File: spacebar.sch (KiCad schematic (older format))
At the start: 5 parts

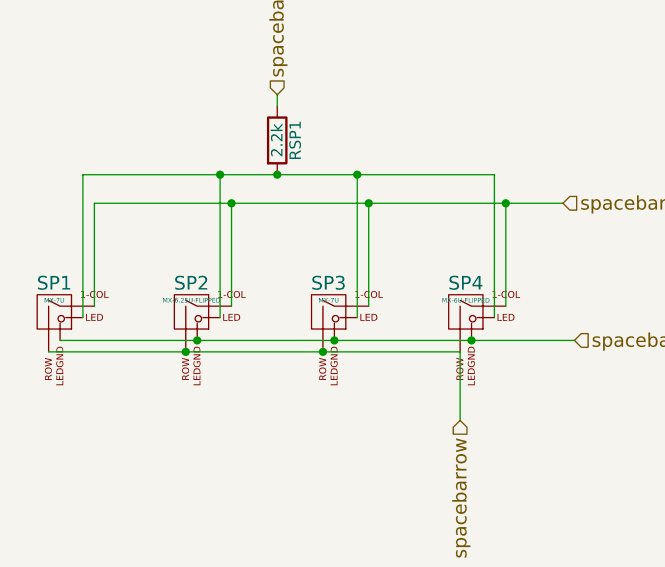
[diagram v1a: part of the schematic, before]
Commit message: Fix all key annotations
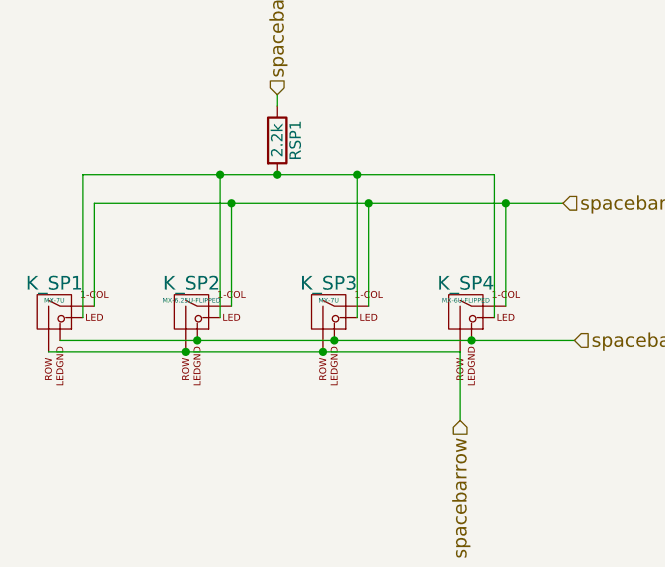
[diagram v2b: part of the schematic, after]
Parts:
- renumbered SP1 to K_SP1, SP2 to K_SP2, SP3 to K_SP3, SP4 to K_SP4
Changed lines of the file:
@@
 $EndDescr
 $Comp
-L MX-7U SP1
+L MX-7U K_SP1
 U 1 1 59353DBD
 P 3825 3400
-F 0 "SP1" H 3825 3525 60  0000 C CNN
+F 0 "K_SP1" H 3825 3525 60  0000 C CNN
 F 1 "MX-7U" H 3825 3450 20  0000 C CNN
 F 2 "" H 3800 3375 60  0001 C CNN
@@
 $EndComp
 $Comp
-L MX-7U SP3
+L MX-7U K_SP3
 U 1 1 59353E7D
 P 5025 3400
-F 0 "SP3" H 5025 3525 60  0000 C CNN
+F 0 "K_SP3" H 5025 3525 60  0000 C CNN
 F 1 "MX-7U" H 5025 3450 20  0000 C CNN
 F 2 "" H 5000 3375 60  0001 C CNN
@@
 	4800 2500 4800 2450
 $Comp
-L MX-6.25U-FLIPPED SP2
+L MX-6.25U-FLIPPED K_SP2
 U 1 1 593599DE
 P 4425 3400
-F 0 "SP2" H 4425 3525 60  0000 C CNN
+F 0 "K_SP2" H 4425 3525 60  0000 C CNN
 F 1 "MX-6.25U-FLIPPED" H 4425 3450 20  0000 C CNN
 F 2 "" H 4400 3375 60  0001 C CNN
@@
 Connection ~ 4450 3525
 $Comp
-L MX-6U-FLIPPED SP4
+L MX-6U-FLIPPED K_SP4
 U 1 1 59359F3B
 P 5625 3400
-F 0 "SP4" H 5625 3525 60  0000 C CNN
+F 0 "K_SP4" H 5625 3525 60  0000 C CNN
 F 1 "MX-6U-FLIPPED" H 5625 3450 20  0000 C CNN
 F 2 "" H 5600 3375 60  0001 C CNN

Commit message: Fix left shift, associate MX footprints
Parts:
- K_SP1, K_SP3: footprint (none) -> MX_Alps_Hybrid:MX-7U-ReversedStabilizers
- K_SP2: footprint (none) -> MX_Alps_Hybrid:MX-6.25U-ReversedStabilizers
- K_SP4: footprint (none) -> MX_Alps_Hybrid:MX-6U-ReversedStabilizers
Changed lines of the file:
@@
 F 0 "K_SP1" H 3825 3525 60  0000 C CNN
 F 1 "MX-7U" H 3825 3450 20  0000 C CNN
-F 2 "" H 3800 3375 60  0001 C CNN
+F 2 "MX_Alps_Hybrid:MX-7U-ReversedStabilizers" H 3800 3375 60  0001 C CNN
 F 3 "" H 3800 3375 60  0001 C CNN
 	1    3825 3400
@@
 F 0 "K_SP3" H 5025 3525 60  0000 C CNN
 F 1 "MX-7U" H 5025 3450 20  0000 C CNN
-F 2 "" H 5000 3375 60  0001 C CNN
+F 2 "MX_Alps_Hybrid:MX-7U-ReversedStabilizers" H 5000 3375 60  0001 C CNN
 F 3 "" H 5000 3375 60  0001 C CNN
 	1    5025 3400
@@
 F 0 "K_SP2" H 4425 3525 60  0000 C CNN
 F 1 "MX-6.25U-FLIPPED" H 4425 3450 20  0000 C CNN
-F 2 "" H 4400 3375 60  0001 C CNN
+F 2 "MX_Alps_Hybrid:MX-6.25U-ReversedStabilizers" H 4400 3375 60  0001 C CNN
 F 3 "" H 4400 3375 60  0001 C CNN
 	1    4425 3400
@@
 F 0 "K_SP4" H 5625 3525 60  0000 C CNN
 F 1 "MX-6U-FLIPPED" H 5625 3450 20  0000 C CNN
-F 2 "" H 5600 3375 60  0001 C CNN
+F 2 "MX_Alps_Hybrid:MX-6U-ReversedStabilizers" H 5600 3375 60  0001 C CNN
 F 3 "" H 5600 3375 60  0001 C CNN
 	1    5625 3400

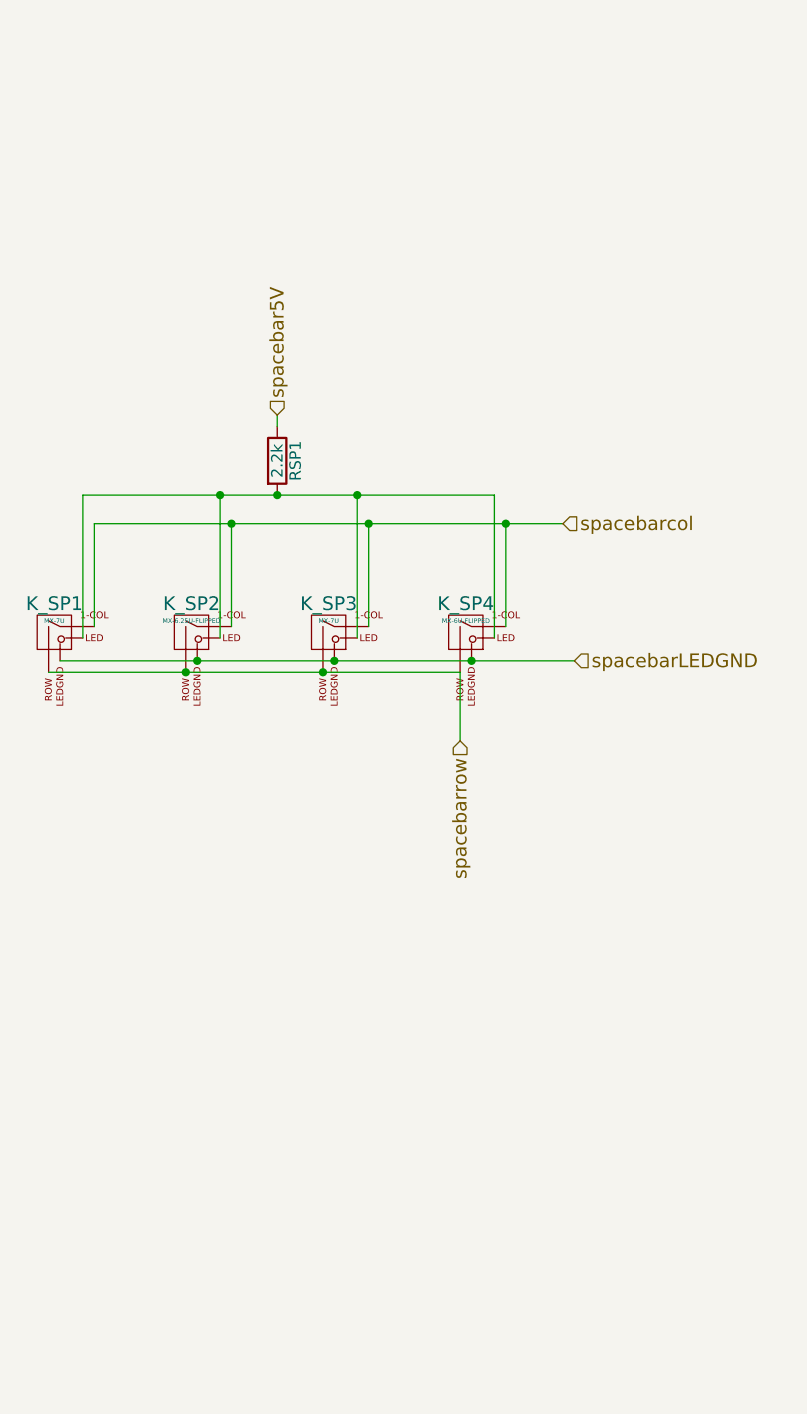
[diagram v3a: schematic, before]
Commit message: Added most spacebar schematics
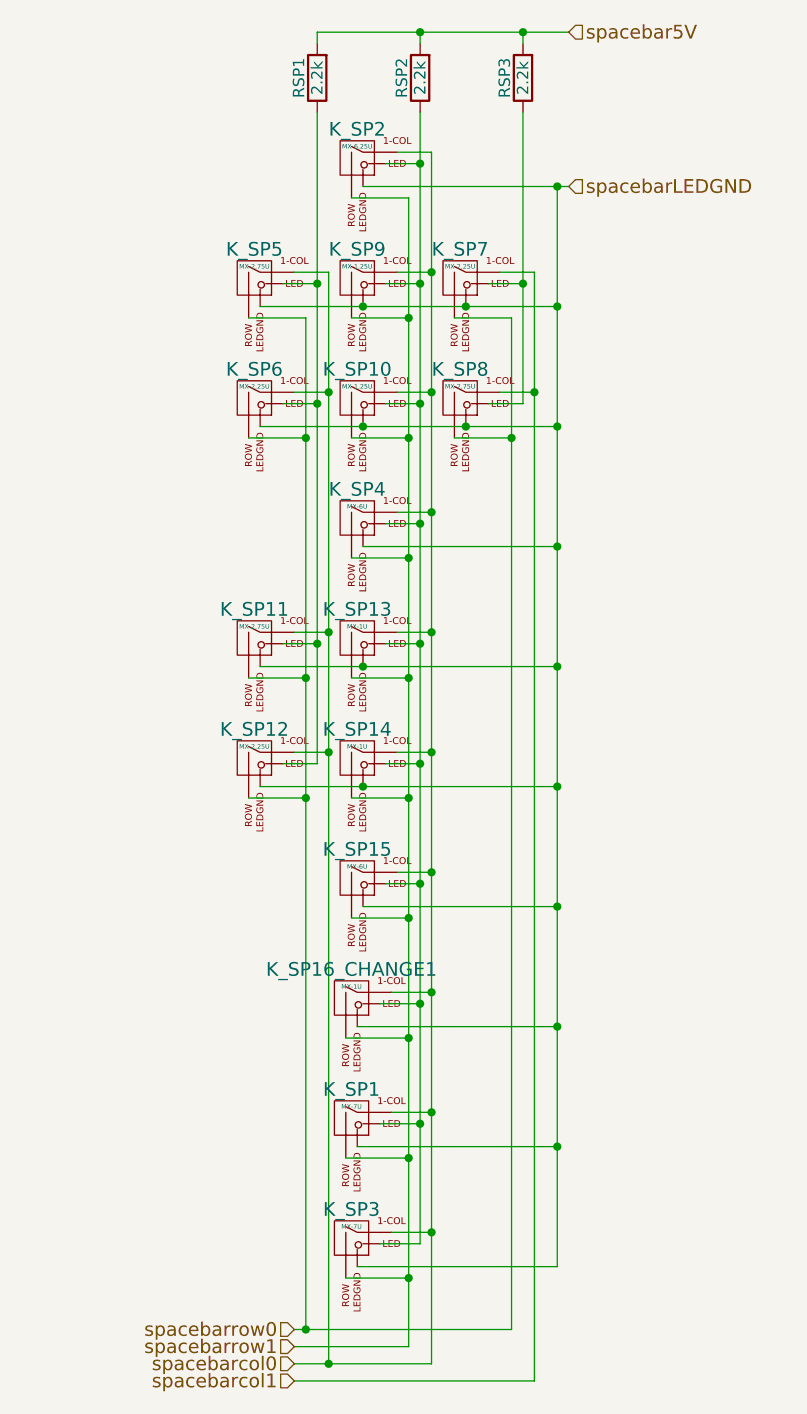
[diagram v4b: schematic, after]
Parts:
- removed K_SP2: MX-6.25U-FLIPPED, MX_Alps_Hybrid:MX-6.25U-ReversedStabilizers, symbol MX-6.25U-FLIPPED
- removed K_SP4: MX-6U-FLIPPED, MX_Alps_Hybrid:MX-6U-ReversedStabilizers, symbol MX-6U-FLIPPED
- added K_SP10, K_SP9: MX-1.25U, MX_Alps_Hybrid:MX-1.25U, symbol MX-1.25U
- added K_SP11, K_SP5, K_SP8: MX-2.75U, MX_Alps_Hybrid:MX-2.75U, symbol MX-2.75U
- added K_SP12, K_SP7: MX-2.25U, MX_Alps_Hybrid:MX-2.25U, symbol MX-2.25U
- added K_SP13, K_SP14: MX-1U, MX_Alps_Hybrid:MX-1U, symbol MX-1U
- added K_SP15, K_SP4: MX-6U, MX_Alps_Hybrid:MX-6U, symbol MX-6U
- added K_SP16_CHANGE1: MX-1U, symbol MX-1U
- added K_SP2: MX-6.25U, MX_Alps_Hybrid:MX-6.25U, symbol MX-6.25U
- added K_SP6: MX-2.25U, MX_Alps_Hybrid:MX-2.75U, symbol MX-2.25U
- added RSP2, RSP3: 2.2k, symbol R
- K_SP1, K_SP3: footprint MX_Alps_Hybrid:MX-7U-ReversedStabilizers -> MX_Alps_Hybrid:MX-7U
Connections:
- net spacebar5V: now also RSP1.2, RSP2.2, RSP3.2; no longer RSP1.1
- net spacebarLEDGND: now also K_SP10.4 (LEDGND), K_SP11.4 (LEDGND), K_SP12.4 (LEDGND), K_SP13.4 (LEDGND), K_SP14.4 (LEDGND), K_SP15.4 (LEDGND), K_SP16_CHANGE1.4 (LEDGND), K_SP2.4 (LEDGND), K_SP4.4 (LEDGND), K_SP5.4 (LEDGND), K_SP6.4 (LEDGND), K_SP7.4 (LEDGND), K_SP8.4 (LEDGND), K_SP9.4 (LEDGND)
- net at K_SP1.3 (LED), K_SP3.3 (LED): now also K_SP10.3 (LED), K_SP13.3 (LED), K_SP14.3 (LED), K_SP15.3 (LED), K_SP16_CHANGE1.3 (LED), K_SP2.3 (LED), K_SP4.3 (LED), K_SP9.3 (LED), RSP2.1; no longer RSP1.2
- net spacebarcol renamed spacebarcol0
- net spacebarcol0: now also K_SP10.1 (COL), K_SP11.1 (COL), K_SP12.1 (COL), K_SP13.1 (COL), K_SP14.1 (COL), K_SP15.1 (COL), K_SP16_CHANGE1.1 (COL), K_SP2.1 (COL), K_SP4.1 (COL), K_SP5.1 (COL), K_SP6.1 (COL), K_SP9.1 (COL)
- net spacebarrow renamed spacebarrow1
- net spacebarrow1: now also K_SP10.2 (ROW), K_SP13.2 (ROW), K_SP14.2 (ROW), K_SP15.2 (ROW), K_SP16_CHANGE1.2 (ROW), K_SP2.2 (ROW), K_SP4.2 (ROW), K_SP9.2 (ROW)
- new net: K_SP11.3 (LED), K_SP12.3 (LED), K_SP5.3 (LED), K_SP6.3 (LED), RSP1.1
- new net: K_SP7.3 (LED), K_SP8.3 (LED), RSP3.1
- new net spacebarcol1: K_SP7.1 (COL), K_SP8.1 (COL)
- new net spacebarrow0: K_SP11.2 (ROW), K_SP12.2 (ROW), K_SP5.2 (ROW), K_SP6.2 (ROW), K_SP7.2 (ROW), K_SP8.2 (ROW)
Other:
- moved on the sheet: RSP1

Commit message: Added spacebars - need sorting
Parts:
- removed K_SP16_CHANGE1: MX-1U, symbol MX-1U
- added K_SP16: MX-6.5U, MX_Alps_Hybrid:MX-6.5U, symbol MX-6.5U
- K_SP6: footprint MX_Alps_Hybrid:MX-2.75U -> MX_Alps_Hybrid:MX-2.25U
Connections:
- net spacebarLEDGND: now also K_SP16.4 (LEDGND)
- net spacebarcol0: now also K_SP16.1 (COL)
- net spacebarrow1: now also K_SP16.2 (ROW)
- net at K_SP1.3 (LED), K_SP10.3 (LED), K_SP13.3 (LED)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: now also K_SP16.3 (LED)
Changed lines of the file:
@@
 F 0 "K_SP6" H 4700 2500 60  0000 C CNN
 F 1 "MX-2.25U" H 4700 2425 20  0000 C CNN
-F 2 "MX_Alps_Hybrid:MX-2.75U" H 4675 2350 60  0001 C CNN
+F 2 "MX_Alps_Hybrid:MX-2.25U" H 4675 2350 60  0001 C CNN
 F 3 "" H 4675 2350 60  0001 C CNN
 	1    4700 2375
@@
 F 3 "" H 5125 4450 60  0001 C CNN
 	1    5150 4475
-	1    0    0    -1
-$EndComp
-$Comp
-L MX-1U K_SP16_CHANGE1
-U 1 1 594AF1A1
-P 5125 5000
-F 0 "K_SP16_CHANGE1" H 5125 5125 60  0000 C CNN
-F 1 "MX-1U" H 5125 5050 20  0000 C CNN
-F 2 "" H 5100 4975 60  0001 C CNN
-F 3 "" H 5100 4975 60  0001 C CNN
-	1    5125 5000
 	1    0    0    -1
 $EndComp
@@
 	5375 6525 4875 6525
 Connection ~ 4925 6450
+$Comp
+L MX-6.5U K_SP16
+U 1 1 594921F2
+P 5125 5000
+F 0 "K_SP16" H 5125 5125 60  0000 C CNN
+F 1 "MX-6.5U" H 5125 5050 20  0000 C CNN
+F 2 "MX_Alps_Hybrid:MX-6.5U" H 5100 4975 60  0001 C CNN
+F 3 "" H 5100 4975 60  0001 C CNN
+	1    5125 5000
+	1    0    0    -1
+$EndComp
 $EndSCHEMATC

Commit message: Removed duplicate space bars
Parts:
- removed K_SP12: MX-2.25U, MX_Alps_Hybrid:MX-2.25U, symbol MX-2.25U
- removed K_SP16: MX-6.5U, MX_Alps_Hybrid:MX-6.5U, symbol MX-6.5U
- removed K_SP4: MX-6U, MX_Alps_Hybrid:MX-6U, symbol MX-6U
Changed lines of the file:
@@
-$EndComp
-$Comp
-L MX-6U K_SP4
-U 1 1 594AE1CC
-P 5150 2900
-F 0 "K_SP4" H 5150 3025 60  0000 C CNN
-F 1 "MX-6U" H 5150 2950 20  0000 C CNN
-F 2 "MX_Alps_Hybrid:MX-6U" H 5125 2875 60  0001 C CNN
-F 3 "" H 5125 2875 60  0001 C CNN
-	1    5150 2900
-	1    0    0    -1
 $EndComp
 $Comp
@@
 $EndComp
 $Comp
-L MX-2.25U K_SP12
-U 1 1 594AE54A
-P 4700 3950
-F 0 "K_SP12" H 4700 4075 60  0000 C CNN
-F 1 "MX-2.25U" H 4700 4000 20  0000 C CNN
-F 2 "MX_Alps_Hybrid:MX-2.25U" H 4675 3925 60  0001 C CNN
-F 3 "" H 4675 3925 60  0001 C CNN
-	1    4700 3950
-	1    0    0    -1
-$EndComp
-$Comp
 L MX-1U K_SP13
 U 1 1 594AE75E
@@
 	5325 1300 5475 1300
 Wire Wire Line
-	5475 1300 5475 6600
+	5475 6600 5475 1300
 Wire Wire Line
 	5475 1825 5325 1825
@@
 	5575 2025 5825 2025
 Wire Wire Line
-	5825 2025 5825 6450
+	5825 6450 5825 2025
 Wire Wire Line
 	5825 2550 5575 2550
@@
 spacebarcol1
 Wire Wire Line
-	5475 6600 4875 6600
+	4875 6600 5475 6600
 Connection ~ 5025 6600
 Wire Wire Line
 	5925 6675 4875 6675
 Wire Wire Line
-	5825 6450 4875 6450
+	4875 6450 5825 6450
 Wire Wire Line
 	5375 6525 4875 6525
 Connection ~ 4925 6450
-$Comp
-L MX-6.5U K_SP16
-U 1 1 594921F2
-P 5125 5000
-F 0 "K_SP16" H 5125 5125 60  0000 C CNN
-F 1 "MX-6.5U" H 5125 5050 20  0000 C CNN
-F 2 "MX_Alps_Hybrid:MX-6.5U" H 5100 4975 60  0001 C CNN
-F 3 "" H 5100 4975 60  0001 C CNN
-	1    5125 5000
-	1    0    0    -1
-$EndComp
 $EndSCHEMATC

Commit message: added split enter
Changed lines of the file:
@@
 	5325 1300 5475 1300
 Wire Wire Line
-	5475 6600 5475 1300
+	5475 1300 5475 6600
 Wire Wire Line
 	5475 1825 5325 1825
@@
 	5575 2025 5825 2025
 Wire Wire Line
-	5825 6450 5825 2025
+	5825 2025 5825 6450
 Wire Wire Line
 	5825 2550 5575 2550
@@
 spacebarcol1
 Wire Wire Line
-	4875 6600 5475 6600
+	5475 6600 4875 6600
 Connection ~ 5025 6600
 Wire Wire Line
 	5925 6675 4875 6675
 Wire Wire Line
-	4875 6450 5825 6450
+	5825 6450 4875 6450
 Wire Wire Line
 	5375 6525 4875 6525
